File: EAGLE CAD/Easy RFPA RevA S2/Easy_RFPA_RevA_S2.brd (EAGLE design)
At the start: 152.4 x 152.4 mm, 197 parts, among them J101 COAX112640BNC_EDGE, J102 COAX112640BNC_EDGE, J301 COAX112640BNC_EDGE, J302 COAX112640BNC_EDGE, J401 HDR_2X1282836-1282836-1, J402 KK_PCFAN, Q101 IRF520N, Q102 IRF630, Q201 IRF630, Q202 IRF630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

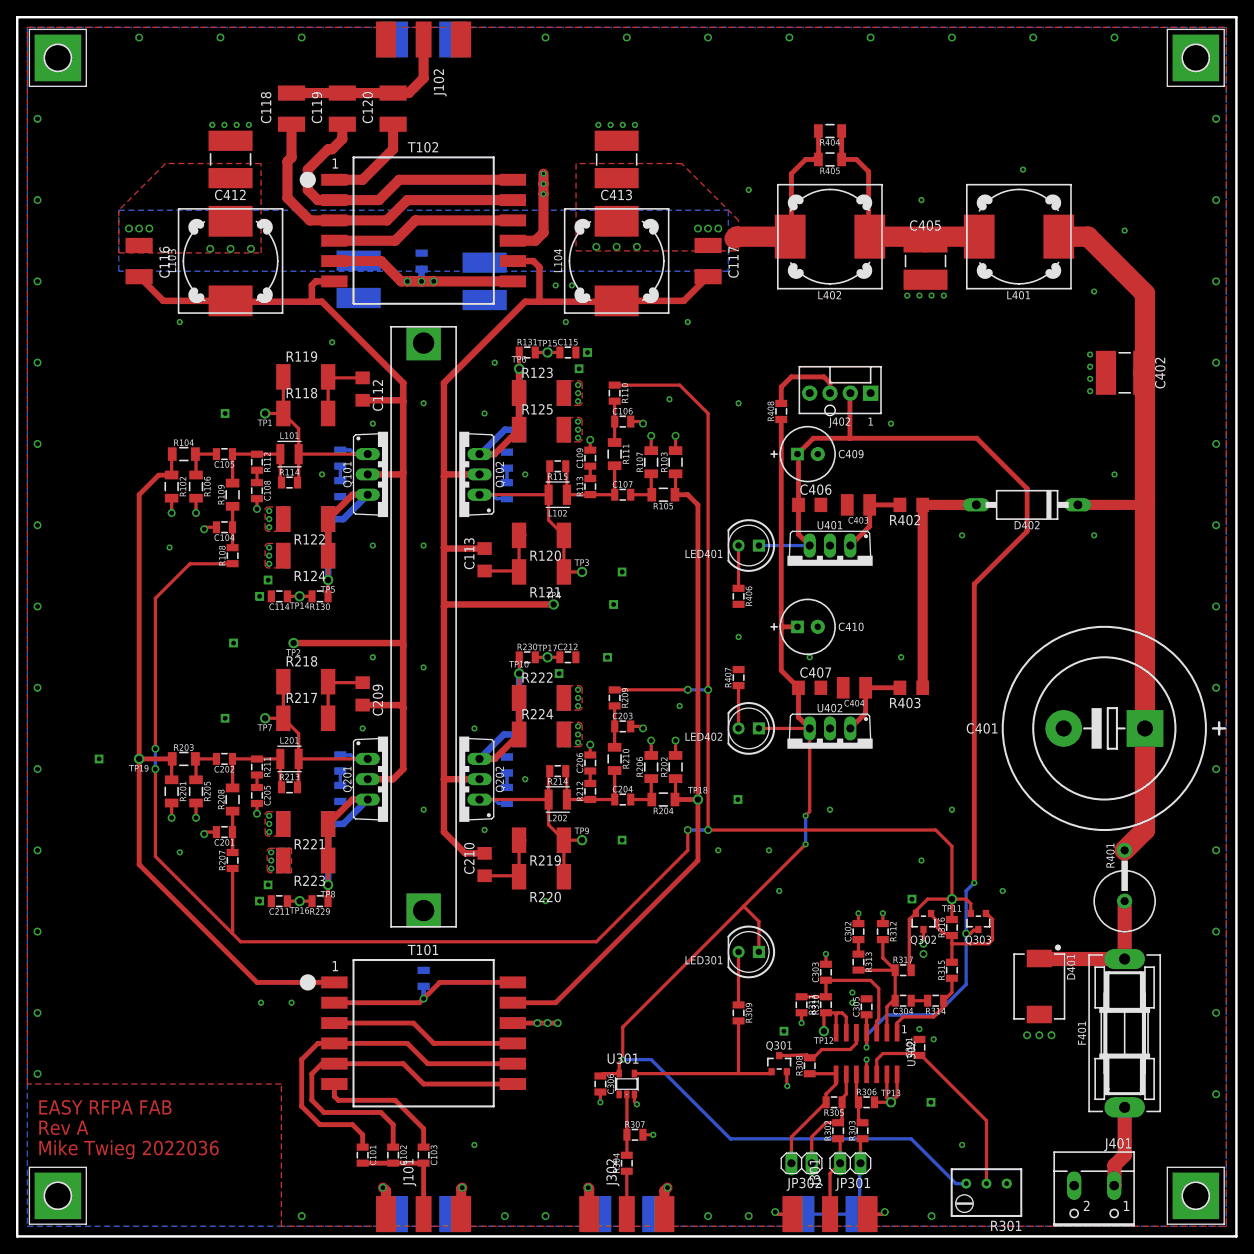
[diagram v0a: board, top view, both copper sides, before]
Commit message: Finishing off revA S2...
Rename files and folder
Fix DRCs errors caused by changing footprints
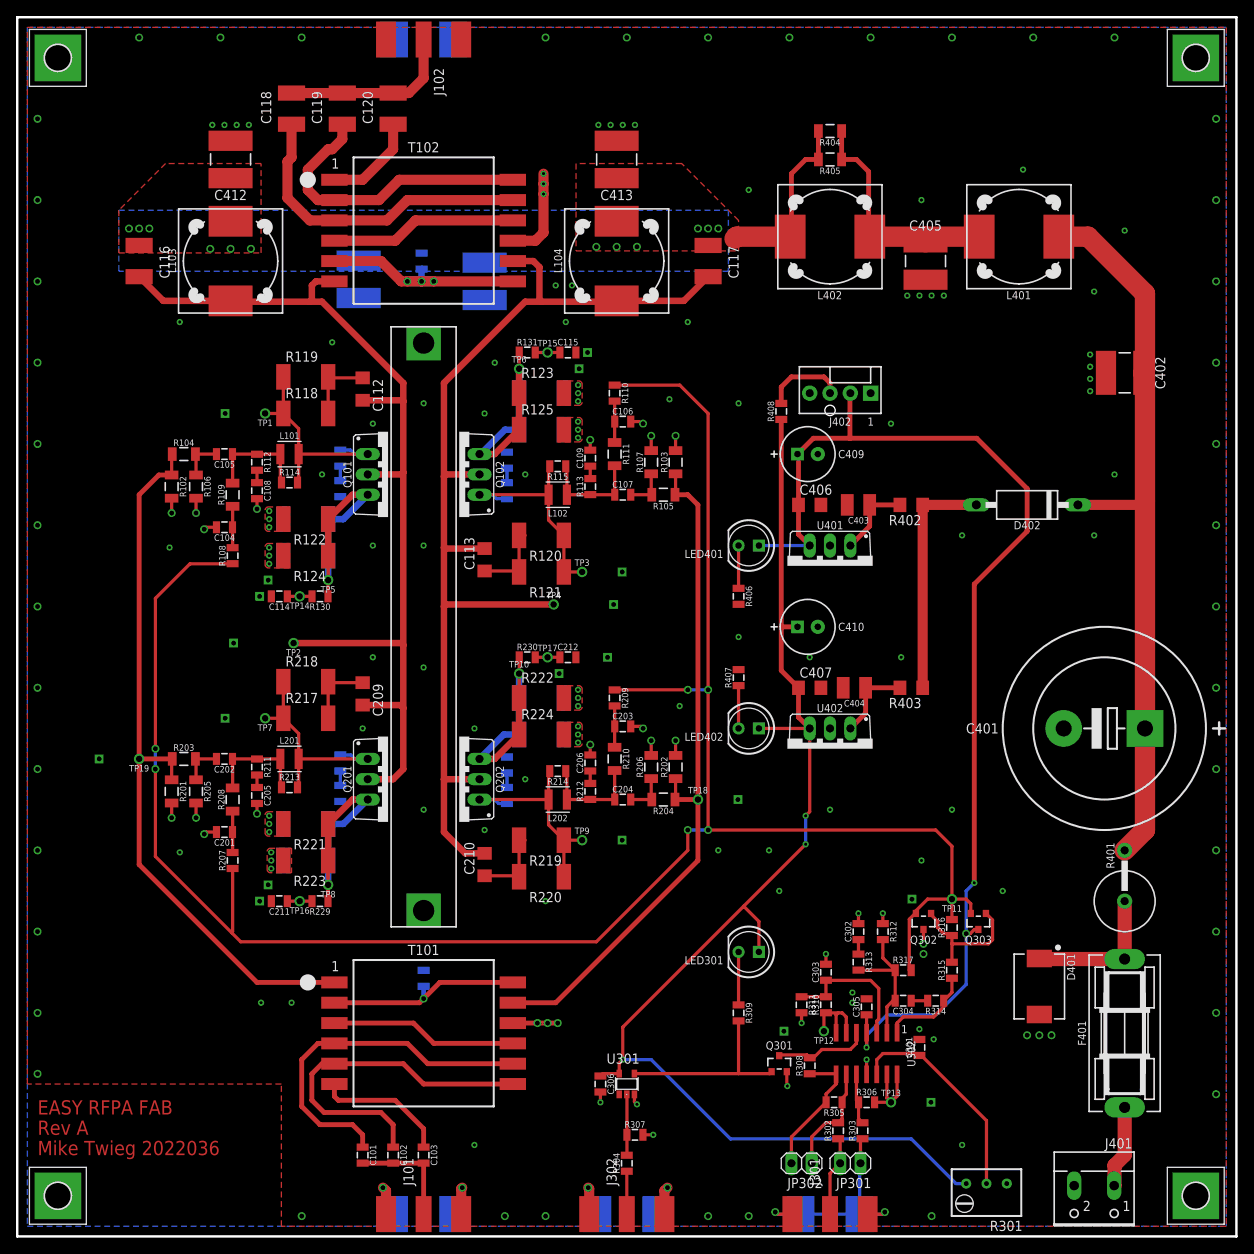
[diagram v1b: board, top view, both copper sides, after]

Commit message: S1 component values
Change component values for S1
Also fix a couple in S2
Export BOM and pdf for S1
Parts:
- C112, C113: value 22nF -> 2.2nF
- R118, R120, R217, R219: value 2.74K -> 330
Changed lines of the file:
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@@
 <attribute name="BOM" value="INCLUDE" x="55.245" y="95.25" size="1.778" layer="27" rot="R90" display="off"/>
 </element>
-<element name="C113" library="MDT_C" package="C1206" value="22nF" x="58.42" y="84.582" rot="R90">
+<element name="C113" library="MDT_C" package="C1206" value="2.2nF" x="58.42" y="84.582" rot="R90">
 <attribute name="PACKAGE" value="1206" x="58.42" y="84.582" size="1.778" layer="27" rot="R90" display="off"/>
 <attribute name="PARTNO" value="" x="58.42" y="84.582" size="1.778" layer="27" rot="R90" display="off"/>
@@
 <attribute name="PACKAGE" value="SOT23-5" x="76.2" y="19.05" size="1.778" layer="27" display="off"/>
 </element>
-<element name="R120" library="MDT_R" package="R2512" value="2.74K" x="65.532" y="87.63" rot="R180">
+<element name="R120" library="MDT_R" package="R2512" value="330" x="65.532" y="87.63" rot="R180">
 <attribute name="PACKAGE" value="2512" x="65.532" y="87.63" size="1.778" layer="27" rot="R180" display="off"/>
 <attribute name="PARTNO" value="" x="65.532" y="87.63" size="1.778" layer="27" rot="R180" display="off"/>
@@
 <attribute name="VENDOR" value="" x="82.296" y="96.774" size="1.778" layer="27" rot="R90" display="off"/>
 </element>
-<element name="C112" library="MDT_C" package="C1206" value="22nF" x="43.18" y="105.918" rot="R270">
+<element name="C112" library="MDT_C" package="C1206" value="2.2nF" x="43.18" y="105.918" rot="R270">
 <attribute name="PACKAGE" value="1206" x="50.8" y="122.174" size="1.778" layer="27" rot="R270" display="off"/>
 <attribute name="PARTNO" value="" x="50.8" y="122.174" size="1.778" layer="27" rot="R270" display="off"/>
@@
 <attribute name="POWER" value="" x="20.828" y="97.79" size="1.778" layer="27" display="off"/>
 </element>
-<element name="R118" library="MDT_R" package="R2512" value="2.74K" x="36.068" y="102.87">
+<element name="R118" library="MDT_R" package="R2512" value="330" x="36.068" y="102.87">
 <attribute name="PACKAGE" value="2512" x="23.876" y="62.23" size="1.778" layer="27" display="off"/>
 <attribute name="PARTNO" value="" x="23.876" y="62.23" size="1.778" layer="27" display="off"/>
@@
 <variant name="IRF520N_20W" populate="no"/>
 </element>
-<element name="R219" library="MDT_R" package="R2512" value="2.74K" x="65.532" y="49.53" rot="R180">
+<element name="R219" library="MDT_R" package="R2512" value="330" x="65.532" y="49.53" rot="R180">
 <attribute name="PACKAGE" value="2512" x="65.532" y="49.53" size="1.778" layer="27" rot="R180" display="off"/>
 <attribute name="PARTNO" value="" x="65.532" y="49.53" size="1.778" layer="27" rot="R180" display="off"/>
@@
 <variant name="IRF520N_20W" populate="no"/>
 </element>
-<element name="R217" library="MDT_R" package="R2512" value="2.74K" x="36.068" y="64.77">
+<element name="R217" library="MDT_R" package="R2512" value="330" x="36.068" y="64.77">
 <attribute name="PACKAGE" value="2512" x="23.876" y="24.13" size="1.778" layer="27" display="off"/>
 <attribute name="PARTNO" value="" x="23.876" y="24.13" size="1.778" layer="27" display="off"/>

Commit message: re-export boms
one of the FETs in S1 had irf520n as the value?
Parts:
- Q101: value IRF520N -> IRF630
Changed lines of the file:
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@@
 </autorouter>
 <elements>
-<element name="Q101" library="MDT_TRANS" package="TO220BV" value="IRF520N" x="46.355" y="95.25" rot="R270">
+<element name="Q101" library="MDT_TRANS" package="TO220BV" value="IRF630" x="46.355" y="95.25" rot="R270">
 <attribute name="PACKAGE" value="TO-220" x="46.355" y="95.25" size="1.778" layer="27" rot="R270" display="off"/>
 <attribute name="CURRENT" value="9A" x="46.355" y="95.25" size="1.778" layer="27" rot="R270" display="off"/>
